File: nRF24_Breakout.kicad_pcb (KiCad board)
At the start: 2 copper layers, 2 parts, among them J1 Conn_01x08_Female, U1 nRF24

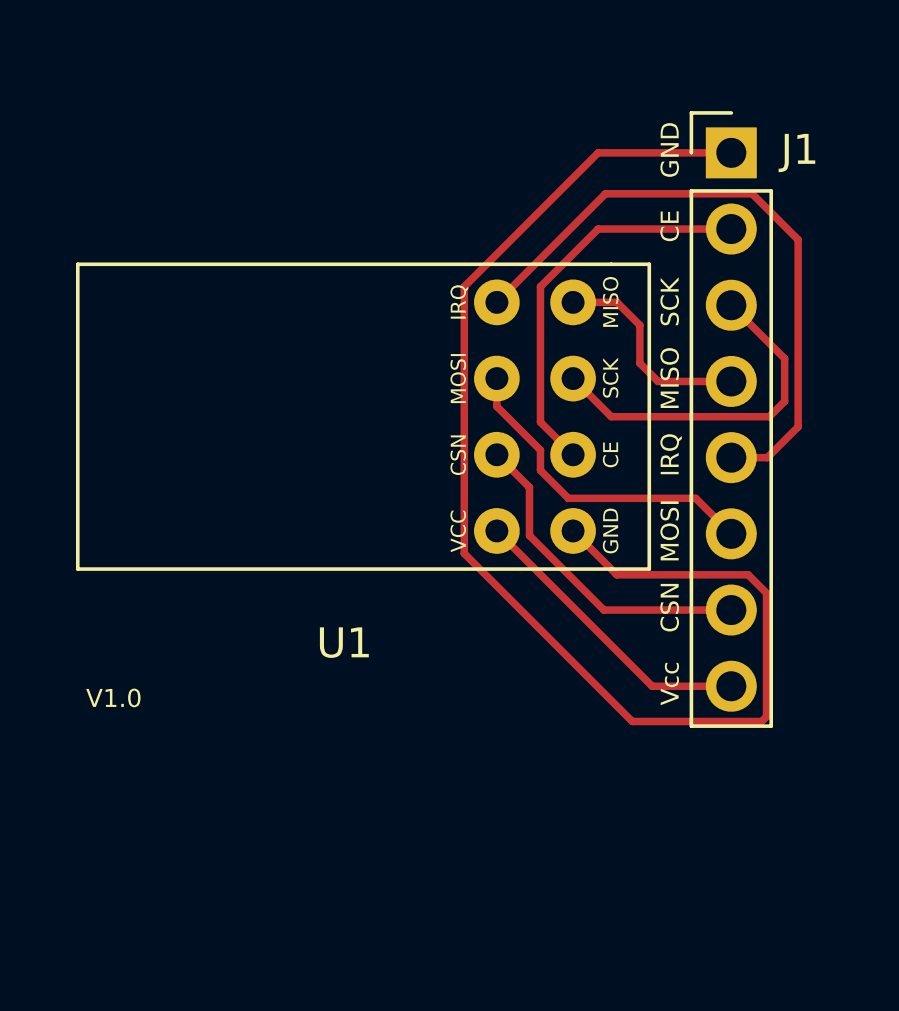
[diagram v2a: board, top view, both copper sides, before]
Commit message: Added filtering cap
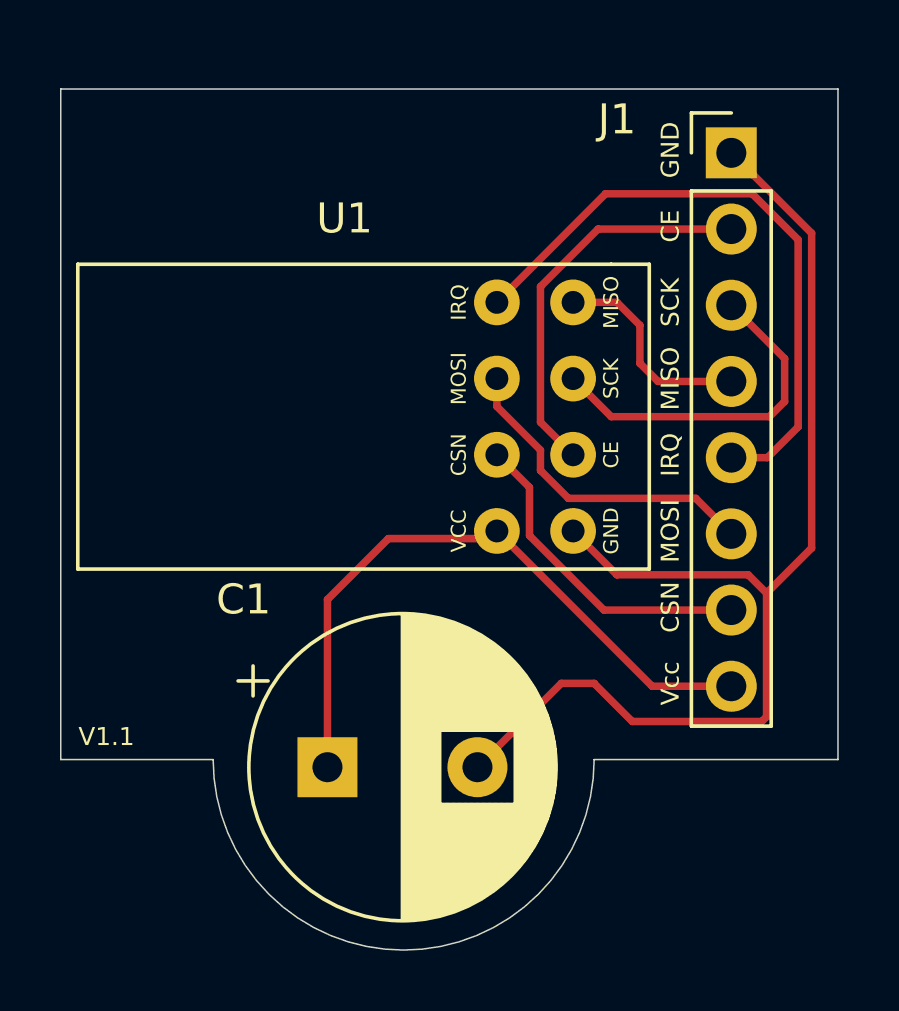
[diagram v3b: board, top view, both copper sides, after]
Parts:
- added C1: 10uF, Capacitor_THT:CP_Radial_D10.0mm_P5.00mm, F.Cu at (138.4, 110.0)
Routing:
- net Net-(C1-Pad1): track 9.96 -> 22.1 mm
- net Net-(C1-Pad2): track 43.5 -> 39.2 mm
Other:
- board outline added: 25.9 x 28.7 mm
- board text added: "V1.1"
- board text removed: "V1.0"

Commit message: Added copper fill
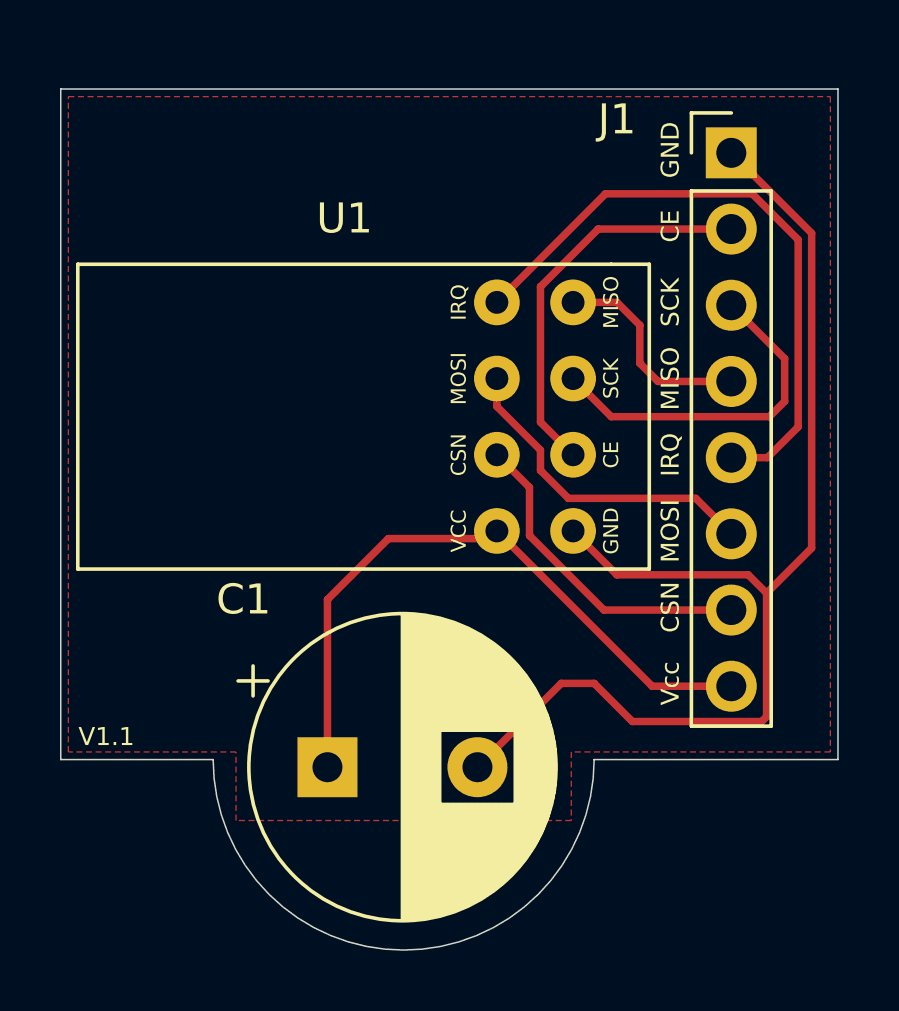
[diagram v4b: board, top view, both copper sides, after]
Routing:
- added copper zone on F.Cu, net Net-(C1-Pad1)
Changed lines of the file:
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@@
   (segment (start 154.570019 92.182019) (end 154.570019 102.676981) (width 0.25) (layer F.Cu) (net 8))
   (segment (start 151.892 89.504) (end 154.570019 92.182019) (width 0.25) (layer F.Cu) (net 8))
+  (zone (net 7) (net_name "Net-(C1-Pad1)") (layer F.Cu) (hatch edge 0.508)
+    (connect_pads (clearance 0.508))
+    (min_thickness 0.254)
+    (fill yes (arc_segments 32) (thermal_gap 0.508) (thermal_bridge_width 0.508))
+    (polygon
+      (pts
+        (xy 155.194 109.474) (xy 146.558 109.474) (xy 146.558 111.76) (xy 135.382 111.76) (xy 135.382 109.474)
+        (xy 129.794 109.474) (xy 129.794 87.63) (xy 155.194 87.63)
+      )
+    )
+  )
 )

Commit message: Generated Gerber Files
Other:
- board text added: "nRF24 Breakout"
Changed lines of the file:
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@@
   (general
     (thickness 1.6)
-    (drawings 15)
+    (drawings 20)
     (tracks 48)
     (zones 0)
@@
     (pcbplotparams
       (layerselection 0x010fc_ffffffff)
-      (usegerberextensions false)
+      (usegerberextensions true)
       (usegerberattributes true)
       (usegerberadvancedattributes true)
@@
       (outputformat 1)
       (mirror false)
-      (drillshape 1)
+      (drillshape 0)
       (scaleselection 1)
-      (outputdirectory ""))
+      (outputdirectory "Gerber Export/"))
   )
   (net 0 "")
@@
     )
   )
+  (gr_line (start 130.9243 90.2716) (end 130.9243 88.519) (layer F.SilkS) (width 0.12))
+  (gr_line (start 143.4592 90.2716) (end 130.9243 90.2716) (layer F.SilkS) (width 0.12))
+  (gr_line (start 143.4592 88.519) (end 143.4592 90.2716) (layer F.SilkS) (width 0.12))
+  (gr_line (start 130.9116 88.519) (end 143.4592 88.519) (layer F.SilkS) (width 0.12))
+  (gr_text "nRF24 Breakout" (at 137.16 89.408) (layer F.SilkS)
+    (effects (font (size 1 1) (thickness 0.15)))
+  )
   (gr_arc (start 140.97 109.728) (end 134.62 109.728) (angle -180) (layer Edge.Cuts) (width 0.05))
